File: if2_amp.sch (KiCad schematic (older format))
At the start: 18 parts, among them Q2 Q_NPN_BCE, Q3 Q_NPN_BCE, U3 MCP6D11

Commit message: Receiver test panel ++
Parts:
- removed Q2, Q3: Q_NPN_BCE, symbol Device:Q_NPN_BCE
- added C36: 10n, Capacitor_SMD:C_0805_2012Metric_Pad1.15x1.40mm_HandSolder, symbol Device:C
- added C37, C38: 100n, Capacitor_SMD:C_0805_2012Metric_Pad1.15x1.40mm_HandSolder, symbol Device:C
- added Q2: BC847BS, Package_TO_SOT_SMD:SOT-363_SC-70-6, symbol Transistor_BJT:BC847BS
- added R25: 100, Resistor_SMD:R_0805_2012Metric_Pad1.15x1.40mm_HandSolder, symbol Device:R
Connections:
- wire segments 44 -> 51
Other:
- moved on the sheet: C31, C32, L18, L19, R13, R14, R15, R36, R37, R38, R39

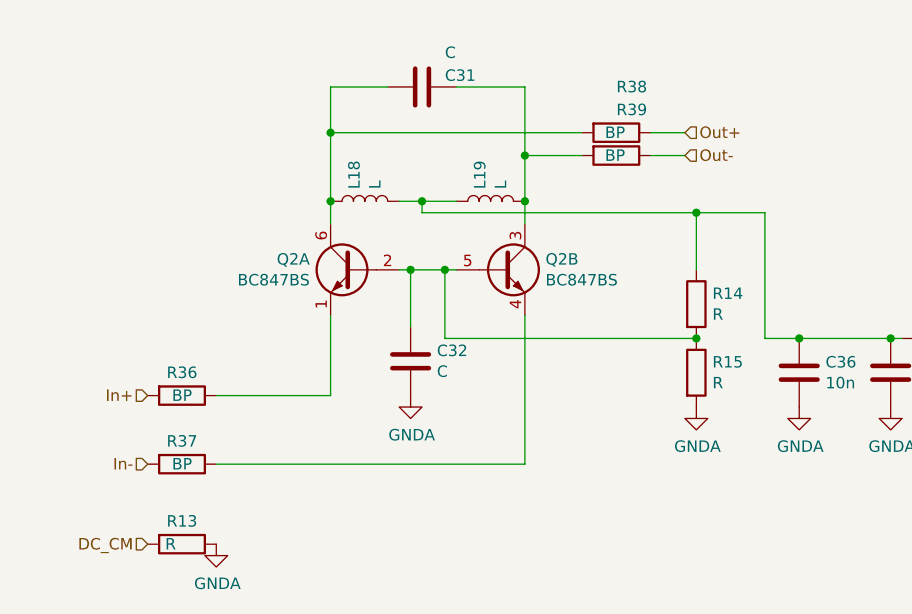
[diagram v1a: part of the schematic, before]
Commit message: IF2 filter and amp recalculate
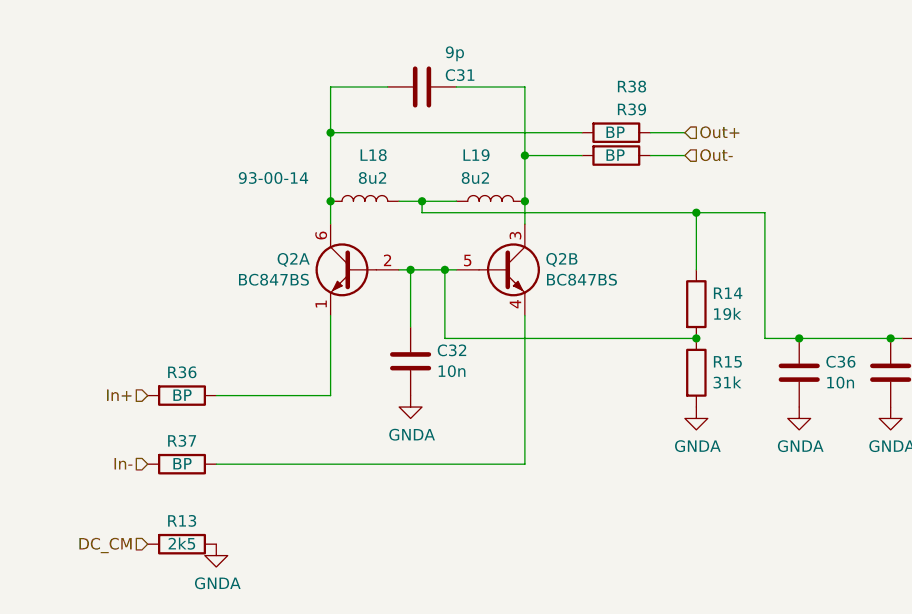
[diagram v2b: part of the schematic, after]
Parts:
- C31: value C -> 9p
- C32: value C -> 10n
- L18: value L -> 8u2; footprint (none) -> Inductor_SMD:L_1210_3225Metric_Pad1.42x2.65mm_HandSolder; Lomex (none) -> 93-00-14
- L19: value L -> 8u2; footprint (none) -> Inductor_SMD:L_1210_3225Metric_Pad1.42x2.65mm_HandSolder
- R13: value R -> 2k5
- R14: value R -> 19k
- R15: value R -> 31k
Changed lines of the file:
@@
 P 7350 3500
 F 0 "C32" H 7465 3546 50  0000 L CNN
-F 1 "C" H 7465 3455 50  0000 L CNN
+F 1 "10n" H 7465 3455 50  0000 L CNN
 F 2 "Capacitor_SMD:C_0805_2012Metric_Pad1.15x1.40mm_HandSolder" H 7388 3350 50  0001 C CNN
 F 3 "~" H 7350 3500 50  0001 C CNN
@@
 P 8600 3250
 F 0 "R14" H 8670 3296 50  0000 L CNN
-F 1 "R" H 8670 3205 50  0000 L CNN
+F 1 "19k" H 8670 3205 50  0000 L CNN
 F 2 "Resistor_SMD:R_0805_2012Metric_Pad1.15x1.40mm_HandSolder" V 8530 3250 50  0001 C CNN
 F 3 "~" H 8600 3250 50  0001 C CNN
@@
 P 8600 3550
 F 0 "R15" H 8670 3596 50  0000 L CNN
-F 1 "R" H 8670 3505 50  0000 L CNN
+F 1 "31k" H 8670 3505 50  0000 L CNN
 F 2 "Resistor_SMD:R_0805_2012Metric_Pad1.15x1.40mm_HandSolder" V 8530 3550 50  0001 C CNN
 F 3 "~" H 8600 3550 50  0001 C CNN
@@
 U 1 1 5FEC71FC
 P 7150 2800
-F 0 "L18" H 7203 2846 50  0000 L CNN
-F 1 "L" H 7203 2755 50  0000 L CNN
-F 2 "" H 7150 2800 50  0001 C CNN
+F 0 "L18" V 7350 2700 50  0000 L CNN
+F 1 "8u2" V 7250 2700 50  0000 L CNN
+F 2 "Inductor_SMD:L_1210_3225Metric_Pad1.42x2.65mm_HandSolder" H 7150 2800 50  0001 C CNN
 F 3 "~" H 7150 2800 50  0001 C CNN
+F 4 "93-00-14" V 7250 3200 50  0000 C CNN "Lomex"
 	1    7150 2800
 	0    -1   -1   0
@@
 P 7400 2300
 F 0 "C31" V 7350 2400 50  0000 L CNN
-F 1 "C" V 7250 2400 50  0000 L CNN
+F 1 "9p" V 7250 2400 50  0000 L CNN
 F 2 "Capacitor_SMD:C_0805_2012Metric_Pad1.15x1.40mm_HandSolder" H 7438 2150 50  0001 C CNN
 F 3 "~" H 7400 2300 50  0001 C CNN
@@
 U 1 1 5FEC838F
 P 7700 2800
-F 0 "L19" H 7753 2846 50  0000 L CNN
-F 1 "L" H 7753 2755 50  0000 L CNN
-F 2 "" H 7700 2800 50  0001 C CNN
+F 0 "L19" V 7900 2800 50  0000 L CNN
+F 1 "8u2" V 7800 2800 50  0000 L CNN
+F 2 "Inductor_SMD:L_1210_3225Metric_Pad1.42x2.65mm_HandSolder" H 7700 2800 50  0001 C CNN
 F 3 "~" H 7700 2800 50  0001 C CNN
 	1    7700 2800
@@
 P 6350 4300
 F 0 "R13" V 6250 4300 50  0000 C CNN
-F 1 "R" V 6350 4250 50  0000 C CNN
+F 1 "2k5" V 6350 4300 50  0000 C CNN
 F 2 "Resistor_SMD:R_0805_2012Metric_Pad1.15x1.40mm_HandSolder" V 6280 4300 50  0001 C CNN
 F 3 "~" H 6350 4300 50  0001 C CNN

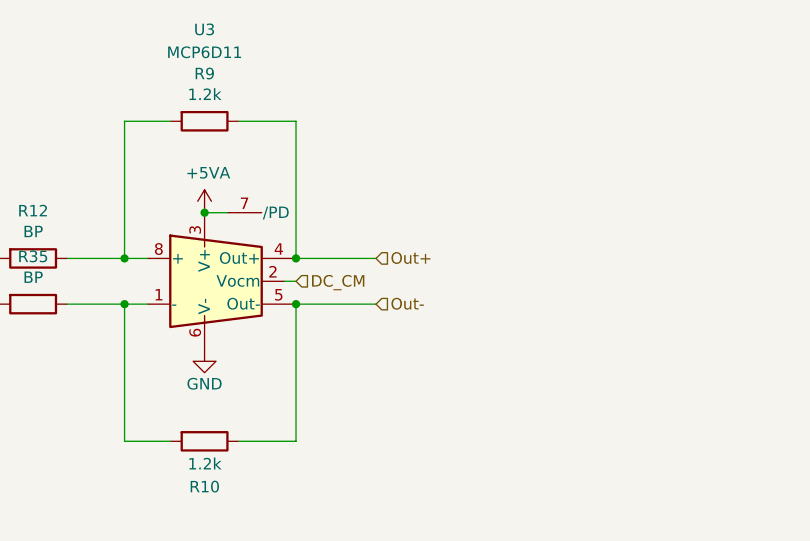
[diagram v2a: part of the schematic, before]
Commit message: if2amp BP resistor added
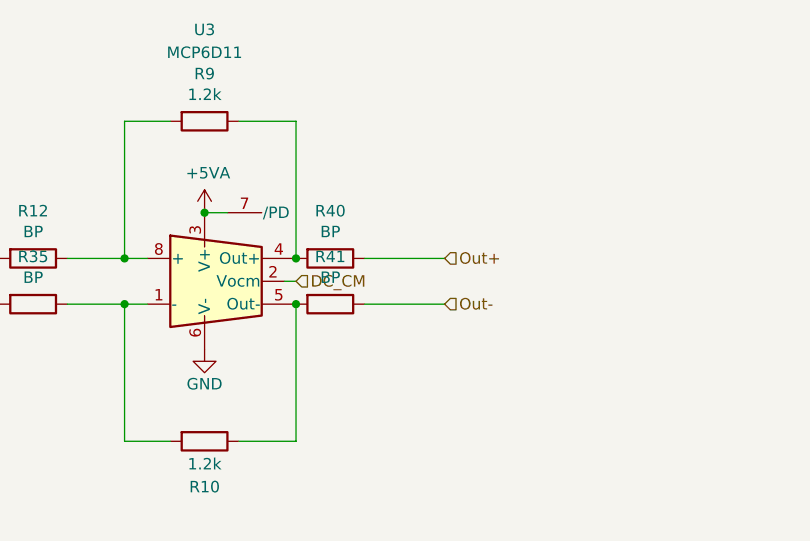
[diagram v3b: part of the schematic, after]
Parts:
- added R40, R41: BP, Resistor_SMD:R_1206_3216Metric_Pad1.42x1.75mm_HandSolder, symbol Device:R
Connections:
- net Out+: now also R40.1; no longer R9.1, U3.4 (Out+)
- net Out-: now also R41.1; no longer R10.1, U3.5 (Out-)
- new net: R40.2, R9.1, U3.4 (Out+)
- new net: R10.1, R41.2, U3.5 (Out-)
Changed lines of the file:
@@
 Wire Wire Line
 	2800 2450 2550 2450
-Text HLabel 3150 3050 2    50   Input ~ 0
+Text HLabel 3450 3050 2    50   Input ~ 0
 Out+
-Text HLabel 3150 3250 2    50   Input ~ 0
+Text HLabel 3450 3250 2    50   Input ~ 0
 Out-
 Wire Wire Line
-	3150 3050 2800 3050
-Connection ~ 2800 3050
-Wire Wire Line
-	2800 3250 3150 3250
-Connection ~ 2800 3250
+	3450 3050 3100 3050
+Wire Wire Line
+	3100 3250 3450 3250
 Wire Wire Line
 	2800 3150 2750 3150
@@
 Wire Wire Line
 	6500 3650 7000 3650
+$Comp
+L Device:R R40
+U 1 1 6008957E
+P 2950 3050
+F 0 "R40" V 2743 3050 50  0000 C CNN
+F 1 "BP" V 2834 3050 50  0000 C CNN
+F 2 "Resistor_SMD:R_1206_3216Metric_Pad1.42x1.75mm_HandSolder" V 2880 3050 50  0001 C CNN
+F 3 "~" H 2950 3050 50  0001 C CNN
+	1    2950 3050
+	0    1    1    0
+$EndComp
+Connection ~ 2800 3050
+$Comp
+L Device:R R41
+U 1 1 60089A07
+P 2950 3250
+F 0 "R41" V 2743 3250 50  0000 C CNN
+F 1 "BP" V 2834 3250 50  0000 C CNN
+F 2 "Resistor_SMD:R_1206_3216Metric_Pad1.42x1.75mm_HandSolder" V 2880 3250 50  0001 C CNN
+F 3 "~" H 2950 3250 50  0001 C CNN
+	1    2950 3250
+	0    1    1    0
+$EndComp
+Connection ~ 2800 3250
 $EndSCHEMATC

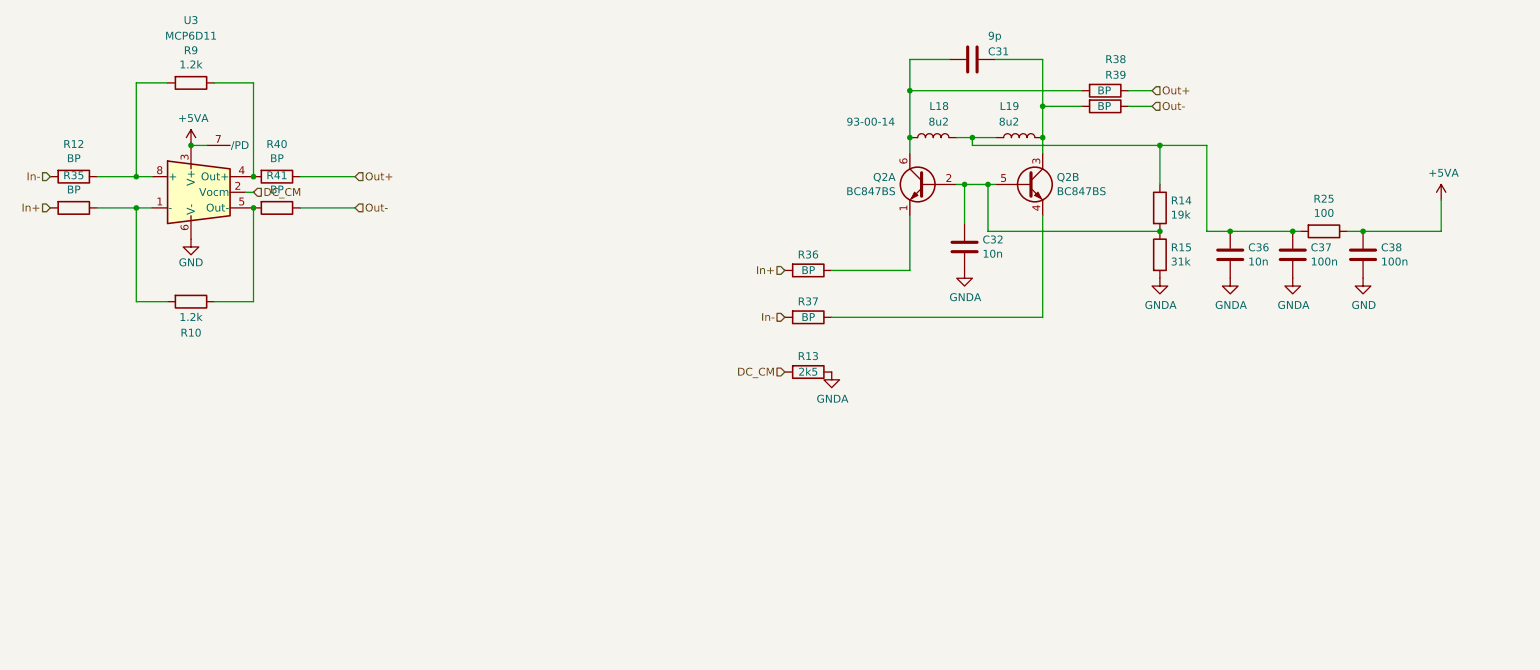
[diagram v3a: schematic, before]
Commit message: if2_bpf revised + Schematic cleanup
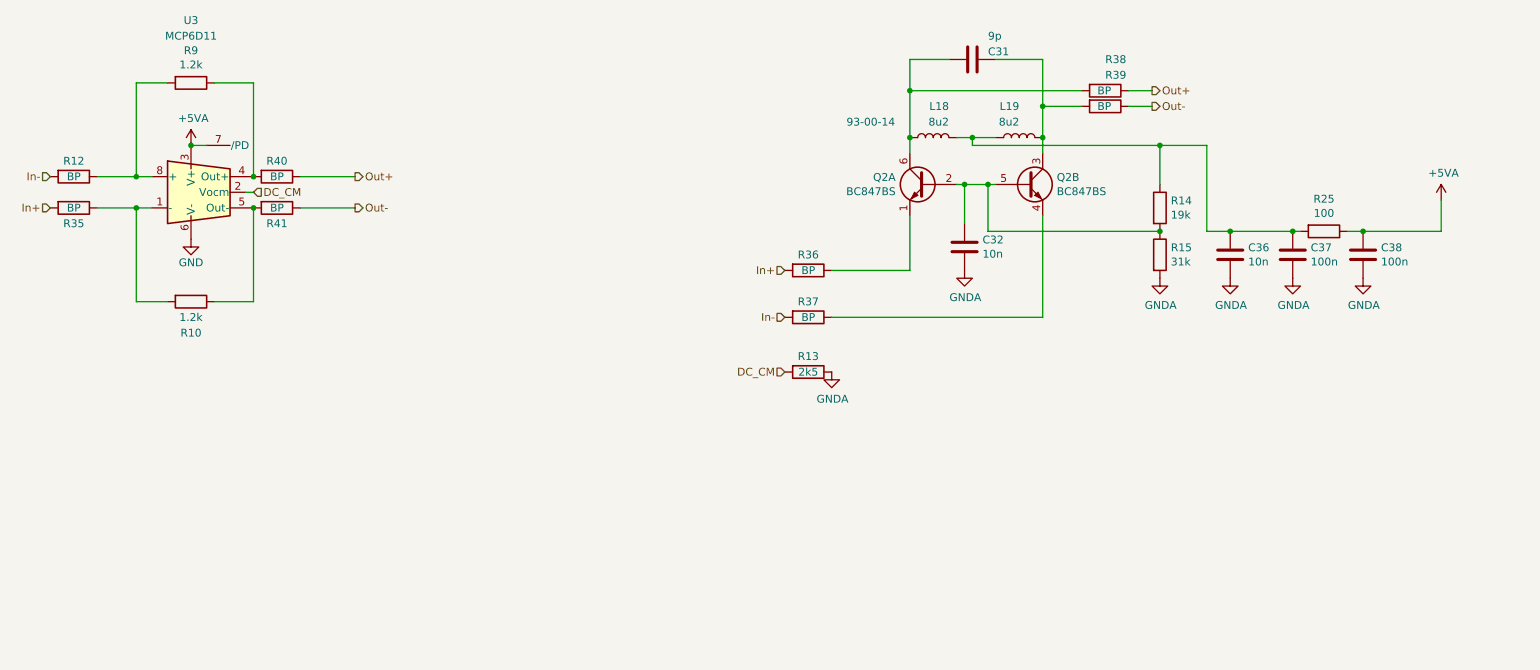
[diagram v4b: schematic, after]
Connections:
- net GND: no longer C38.2
- net GNDA: now also C38.2
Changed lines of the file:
@@
 Wire Wire Line
 	2800 2450 2550 2450
-Text HLabel 3450 3050 2    50   Input ~ 0
+Text HLabel 3450 3050 2    50   Output ~ 0
 Out+
-Text HLabel 3450 3250 2    50   Input ~ 0
+Text HLabel 3450 3250 2    50   Output ~ 0
 Out-
 Wire Wire Line
@@
 U 1 1 5FFCBAF5
 P 1650 3050
-F 0 "R12" V 1443 3050 50  0000 C CNN
-F 1 "BP" V 1534 3050 50  0000 C CNN
+F 0 "R12" V 1550 3050 50  0000 C CNN
+F 1 "BP" V 1650 3050 50  0000 C CNN
 F 2 "Resistor_SMD:R_1206_3216Metric_Pad1.42x1.75mm_HandSolder" V 1580 3050 50  0001 C CNN
 F 3 "~" H 1650 3050 50  0001 C CNN
@@
 U 1 1 5FFCD24E
 P 1650 3250
-F 0 "R35" V 1443 3250 50  0000 C CNN
-F 1 "BP" V 1534 3250 50  0000 C CNN
+F 0 "R35" V 1750 3250 50  0000 C CNN
+F 1 "BP" V 1650 3250 50  0000 C CNN
 F 2 "Resistor_SMD:R_1206_3216Metric_Pad1.42x1.75mm_HandSolder" V 1580 3250 50  0001 C CNN
 F 3 "~" H 1650 3250 50  0001 C CNN
@@
 Wire Wire Line
 	6500 3950 7850 3950
-Text HLabel 8550 2500 2    50   Input ~ 0
+Text HLabel 8550 2500 2    50   Output ~ 0
 Out+
-Text HLabel 8550 2600 2    50   Input ~ 0
+Text HLabel 8550 2600 2    50   Output ~ 0
 Out-
 $Comp
@@
 	1    0    0    -1
 $EndComp
-$Comp
-L power:GND #PWR?
-U 1 1 6013F264
-P 9900 3700
-AR Path="/5FE332ED/6013F264" Ref="#PWR?"  Part="1"
-AR Path="/5FE3342F/6013F264" Ref="#PWR0143"  Part="1"
-F 0 "#PWR0143" H 9900 3450 50  0001 C CNN
-F 1 "GND" H 9905 3527 50  0000 C CNN
-F 2 "" H 9900 3700 50  0001 C CNN
-F 3 "" H 9900 3700 50  0001 C CNN
-	1    9900 3700
-	1    0    0    -1
-$EndComp
 Wire Wire Line
 	9900 3400 9800 3400
@@
 U 1 1 6008957E
 P 2950 3050
-F 0 "R40" V 2743 3050 50  0000 C CNN
-F 1 "BP" V 2834 3050 50  0000 C CNN
+F 0 "R40" V 2850 3050 50  0000 C CNN
+F 1 "BP" V 2950 3050 50  0000 C CNN
 F 2 "Resistor_SMD:R_1206_3216Metric_Pad1.42x1.75mm_HandSolder" V 2880 3050 50  0001 C CNN
 F 3 "~" H 2950 3050 50  0001 C CNN
@@
 U 1 1 60089A07
 P 2950 3250
-F 0 "R41" V 2743 3250 50  0000 C CNN
-F 1 "BP" V 2834 3250 50  0000 C CNN
+F 0 "R41" V 3050 3250 50  0000 C CNN
+F 1 "BP" V 2950 3250 50  0000 C CNN
 F 2 "Resistor_SMD:R_1206_3216Metric_Pad1.42x1.75mm_HandSolder" V 2880 3250 50  0001 C CNN
 F 3 "~" H 2950 3250 50  0001 C CNN
@@
 $EndComp
 Connection ~ 2800 3250
+$Comp
+L power:GNDA #PWR?
+U 1 1 601B57DB
+P 9900 3700
+AR Path="/5FE332ED/601B57DB" Ref="#PWR?"  Part="1"
+AR Path="/5FE3342F/601B57DB" Ref="#PWR?"  Part="1"
+F 0 "#PWR?" H 9900 3450 50  0001 C CNN
+F 1 "GNDA" H 9905 3527 50  0000 C CNN
+F 2 "" H 9900 3700 50  0001 C CNN
+F 3 "" H 9900 3700 50  0001 C CNN
+	1    9900 3700
+	1    0    0    -1
+$EndComp
 $EndSCHEMATC
